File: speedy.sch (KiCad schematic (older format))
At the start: 37 parts, among them U1 STM32F415RGT6, U2 NUF2042VX6, X1 16Mhz 10ppm

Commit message: Change micro USB connector & add 3d models to some footprints
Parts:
- CONN4: footprint _connectors:_Micro-USB-AB-receptacle-SMT -> _connectors:_Micro-USB-AB-receptacle-SMT-th
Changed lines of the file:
@@
 F 0 "CONN4" H 8375 1850 60  0000 C CNN
 F 1 "MICRO_USB" H 8425 1050 60  0000 C CNN
-F 2 "_connectors:_Micro-USB-AB-receptacle-SMT" H 8375 1450 60  0001 C CNN
+F 2 "_connectors:_Micro-USB-AB-receptacle-SMT-th" H 8375 1450 60  0001 C CNN
 F 3 "" H 8375 1450 60  0000 C CNN
 	1    8375 1450

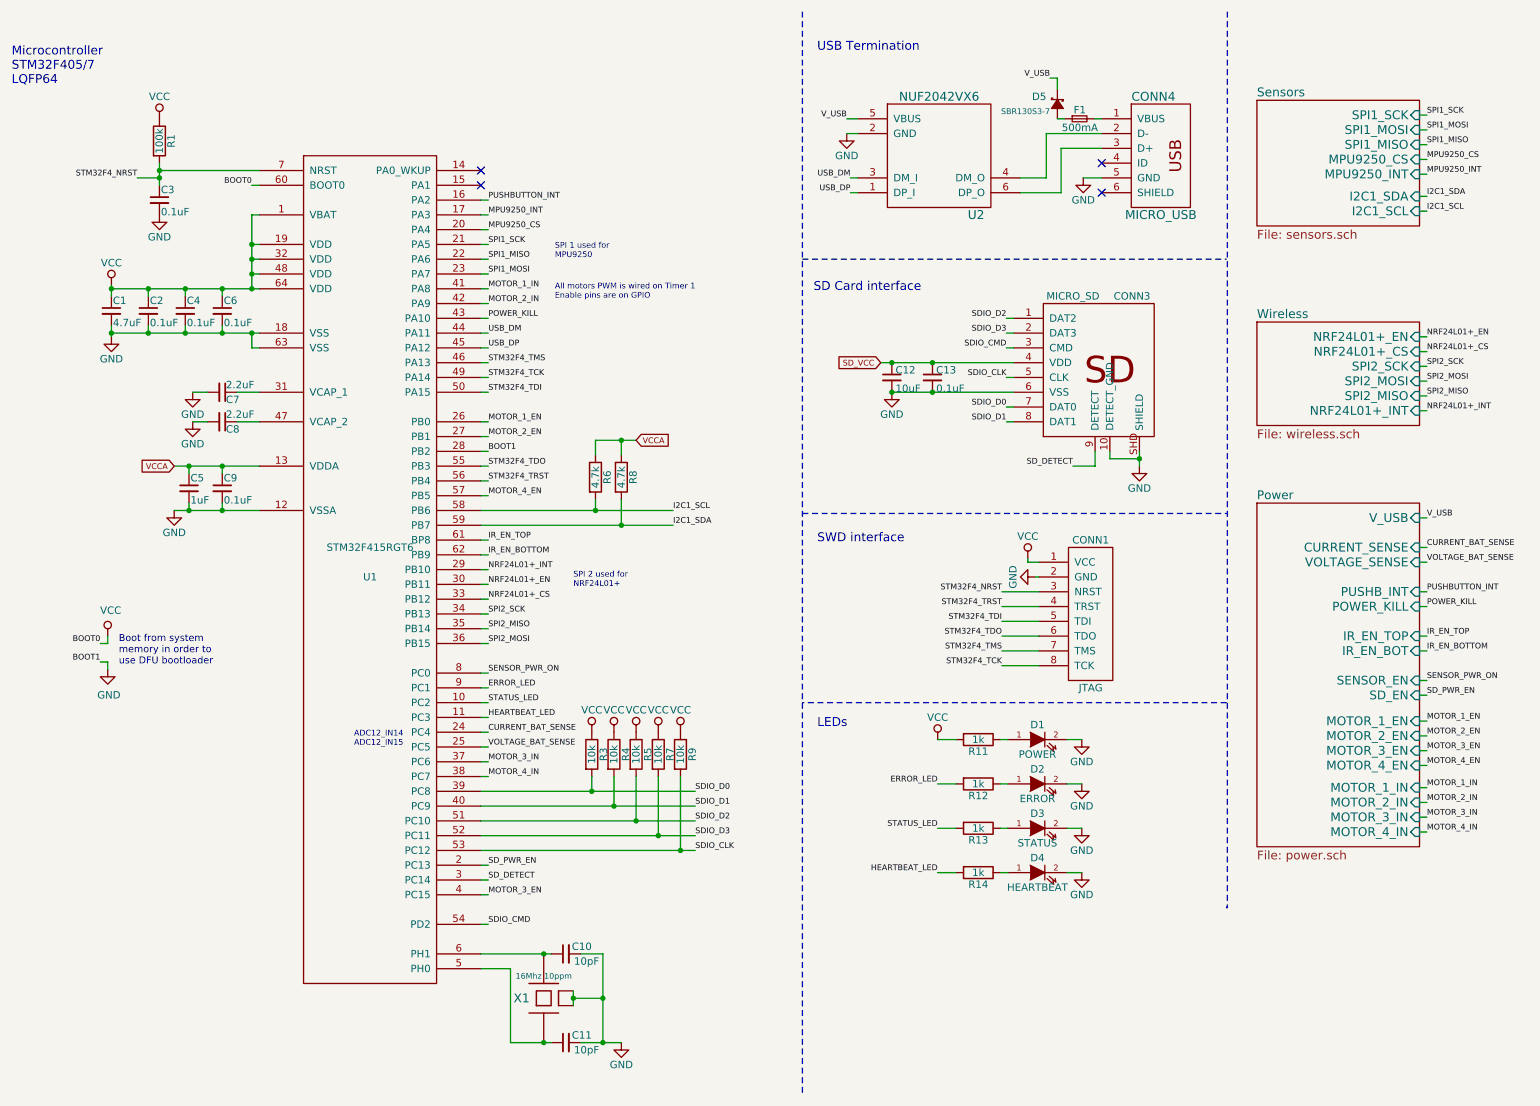
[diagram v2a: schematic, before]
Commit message: Move SDIO pullups from clock to CMD
see NXP AN10911 http://www.nxp.com/documents/application_note/AN10911.pdf
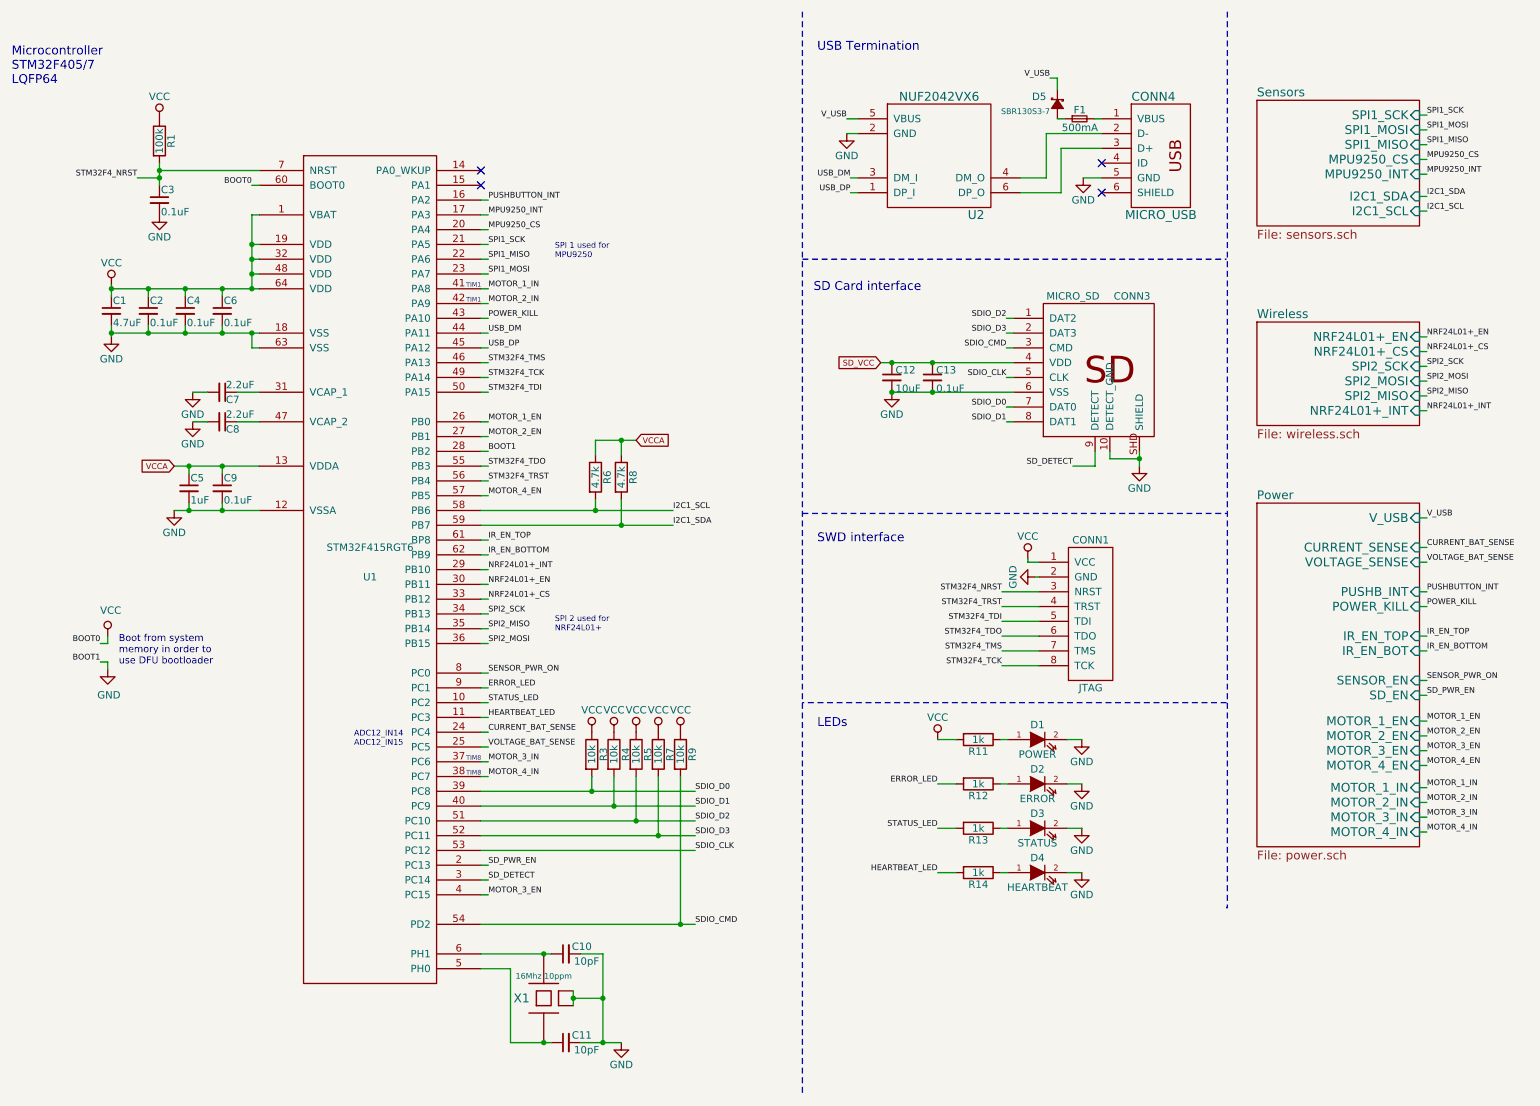
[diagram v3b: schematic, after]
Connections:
- net SDIO_CLK: no longer R9.2
- net SDIO_CMD: now also R9.2
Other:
- note added: "TIM1"
- note added: "TIM8"
- note removed: "All motors PWM is wired on Timer 1\nEnable pins are on GPIO"
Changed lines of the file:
@@
 Text Label 5275 6150 0    39   ~ 0
 SDIO_CLK
-Text Label 3875 6650 0    39   ~ 0
+Text Label 5275 6650 0    39   ~ 0
 SDIO_CMD
 Text Label 3875 6350 0    39   ~ 0
@@
 $EndComp
 $Comp
-L R R9
-U 1 1 5538B6D0
-P 5175 5500
-F 0 "R9" V 5255 5500 50  0000 C CNN
-F 1 "10k" V 5175 5500 50  0000 C CNN
-F 2 "_std:_0402" V 5105 5500 30  0001 C CNN
-F 3 "" H 5175 5500 30  0000 C CNN
-	1    5175 5500
-	1    0    0    -1
-$EndComp
-$Comp
 L VCC #PWR012
 U 1 1 5538C13D
@@
 F 3 "" H 5025 5350 60  0000 C CNN
 	1    5025 5350
-	1    0    0    -1
-$EndComp
-$Comp
-L VCC #PWR016
-U 1 1 5538C2E9
-P 5175 5350
-F 0 "#PWR016" H 5175 5200 50  0001 C CNN
-F 1 "VCC" H 5175 5500 50  0000 C CNN
-F 2 "" H 5175 5350 60  0000 C CNN
-F 3 "" H 5175 5350 60  0000 C CNN
-	1    5175 5350
 	1    0    0    -1
 $EndComp
@@
 Text Label 3875 5650 0    39   ~ 0
 MOTOR_4_IN
-Text Notes 4325 2425 0    39   ~ 0
-All motors PWM is wired on Timer 1\nEnable pins are on GPIO
 Text Notes 4325 2150 0    39   ~ 0
 SPI 1 used for \nMPU9250
@@
 Text Label 3875 4250 0    39   ~ 0
 NRF24L01+_INT
-Text Notes 4450 4375 0    39   ~ 0
+Text Notes 4325 4675 0    39   ~ 0
 SPI 2 used for \nNRF24L01+
 $Comp
@@
 	10175 5275 10225 5275
 Wire Wire Line
-	4450 7100 4450 7200
-Connection ~ 5175 6150
-Wire Wire Line
-	5175 5650 5175 6150
+	4450 7100 4450 7150
+Wire Wire Line
+	4450 7150 4450 7200
 Connection ~ 5025 6050
 Wire Wire Line
@@
 	4575 5650 4575 5750
 Wire Wire Line
-	3825 5950 5275 5950
-Wire Wire Line
-	3825 5850 5275 5850
-Wire Wire Line
-	3825 6050 5275 6050
+	3825 5950 4875 5950
+Wire Wire Line
+	4875 5950 5275 5950
+Wire Wire Line
+	3825 5850 4725 5850
+Wire Wire Line
+	4725 5850 5275 5850
+Wire Wire Line
+	3825 6050 5025 6050
+Wire Wire Line
+	5025 6050 5275 6050
 Wire Wire Line
 	3825 6150 5275 6150
 Wire Wire Line
-	3825 6650 3875 6650
-Wire Wire Line
-	3825 5750 5275 5750
+	3825 6650 5175 6650
+Wire Wire Line
+	5175 6650 5275 6650
+Wire Wire Line
+	3825 5750 4575 5750
+Wire Wire Line
+	4575 5750 5275 5750
 Connection ~ 8280 3500
 Wire Wire Line
@@
 	8080 3450 8080 3500
 Wire Wire Line
-	8280 3450 8280 3550
+	8280 3450 8280 3500
+Wire Wire Line
+	8280 3500 8280 3550
 Wire Wire Line
 	7980 3550 7980 3450
@@
 Connection ~ 6880 3050
 Wire Wire Line
-	6605 3050 7430 3050
+	6605 3050 6880 3050
+Wire Wire Line
+	6880 3050 7430 3050
 Connection ~ 6880 2850
 Wire Wire Line
-	6530 2850 7430 2850
+	6530 2850 6605 2850
+Wire Wire Line
+	6605 2850 6880 2850
+Wire Wire Line
+	6880 2850 7430 2850
 Wire Wire Line
 	7380 3250 7430 3250
@@
 	4600 3775 4600 3850
 Wire Wire Line
-	3825 3850 5125 3850
-Wire Wire Line
-	3825 3950 5125 3950
+	3825 3850 4600 3850
+Wire Wire Line
+	4600 3850 5125 3850
+Wire Wire Line
+	3825 3950 4775 3950
+Wire Wire Line
+	4775 3950 5125 3950
 Connection ~ 4250 7450
 Wire Wire Line
@@
 Connection ~ 4650 7450
 Wire Wire Line
-	4500 7450 4775 7450
-Wire Wire Line
-	4650 6850 4650 7450
-Wire Wire Line
-	4025 7450 4300 7450
-Wire Wire Line
-	3825 6850 4300 6850
+	4500 7450 4650 7450
+Wire Wire Line
+	4650 7450 4775 7450
+Wire Wire Line
+	4650 6850 4650 7150
+Wire Wire Line
+	4650 7150 4650 7450
+Wire Wire Line
+	4025 7450 4250 7450
+Wire Wire Line
+	4250 7450 4300 7450
+Wire Wire Line
+	3825 6850 4250 6850
+Wire Wire Line
+	4250 6850 4300 6850
 Connection ~ 1650 1600
 Wire Wire Line
@@
 	1650 1850 1650 1850
 Wire Wire Line
-	1650 1500 1650 1650
+	1650 1500 1650 1550
+Wire Wire Line
+	1650 1550 1650 1600
+Wire Wire Line
+	1650 1600 1650 1650
 Wire Wire Line
 	2325 1550 1650 1550
@@
 Connection ~ 2075 2350
 Wire Wire Line
-	1325 2325 1325 2400
-Wire Wire Line
-	1325 2600 1325 2675
+	1325 2325 1325 2350
+Wire Wire Line
+	1325 2350 1325 2400
+Wire Wire Line
+	1325 2600 1325 2650
+Wire Wire Line
+	1325 2650 1325 2675
 Wire Wire Line
 	1575 2650 1575 2600
@@
 	6000 475  6000 7800
 Wire Wire Line
-	4600 3375 4875 3375
+	4600 3375 4775 3375
+Wire Wire Line
+	4775 3375 4875 3375
 Connection ~ 4775 3375
 Wire Wire Line
@@
 	2325 1850 2275 1850
 Wire Wire Line
-	2275 1850 2275 2350
+	2275 2350 2275 2250
+Wire Wire Line
+	2275 2250 2275 2150
+Wire Wire Line
+	2275 2150 2275 2050
+Wire Wire Line
+	2275 2050 2275 1850
 Connection ~ 2275 2350
 Wire Wire Line
@@
 Connection ~ 2275 2650
 Wire Wire Line
-	1325 2350 2325 2350
-Wire Wire Line
-	1325 2650 2325 2650
+	1325 2350 1575 2350
+Wire Wire Line
+	1575 2350 1825 2350
+Wire Wire Line
+	1825 2350 2075 2350
+Wire Wire Line
+	2075 2350 2275 2350
+Wire Wire Line
+	2275 2350 2325 2350
+Wire Wire Line
+	1325 2650 1575 2650
+Wire Wire Line
+	1575 2650 1825 2650
+Wire Wire Line
+	1825 2650 2075 2650
+Wire Wire Line
+	2075 2650 2275 2650
+Wire Wire Line
+	2275 2650 2325 2650
 Wire Wire Line
 	2175 3050 2325 3050
@@
 	1875 3050 1975 3050
 Wire Wire Line
-	1750 3550 2325 3550
+	1750 3550 1850 3550
+Wire Wire Line
+	1850 3550 2075 3550
+Wire Wire Line
+	2075 3550 2325 3550
 Wire Wire Line
 	1850 3600 1850 3550
@@
 	1850 3800 1850 3850
 Wire Wire Line
-	1750 3850 2325 3850
+	1750 3850 1850 3850
+Wire Wire Line
+	1850 3850 2075 3850
+Wire Wire Line
+	2075 3850 2325 3850
 Wire Wire Line
 	2075 3850 2075 3800
@@
 Text Notes 1375 4900 0    47   ~ 0
 Boot from system\nmemory in order to \nuse DFU bootloader
+Text Notes 3725 5550 0    31   ~ 0
+TIM8
+Text Notes 3725 2350 0    31   ~ 0
+TIM1
+Text Notes 3725 2450 0    31   ~ 0
+TIM1
+Text Notes 3725 5650 0    31   ~ 0
+TIM8
+$Comp
+L VCC #PWR016
+U 1 1 5538C2E9
+P 5175 5350
+F 0 "#PWR016" H 5175 5200 50  0001 C CNN
+F 1 "VCC" H 5175 5500 50  0000 C CNN
+F 2 "" H 5175 5350 60  0000 C CNN
+F 3 "" H 5175 5350 60  0000 C CNN
+	1    5175 5350
+	1    0    0    -1
+$EndComp
+$Comp
+L R R9
+U 1 1 5538B6D0
+P 5175 5500
+F 0 "R9" V 5255 5500 50  0000 C CNN
+F 1 "10k" V 5175 5500 50  0000 C CNN
+F 2 "_std:_0402" V 5105 5500 30  0001 C CNN
+F 3 "" H 5175 5500 30  0000 C CNN
+	1    5175 5500
+	1    0    0    -1
+$EndComp
+Wire Wire Line
+	5175 5650 5175 6650
+Connection ~ 5175 6650
 $EndSCHEMATC

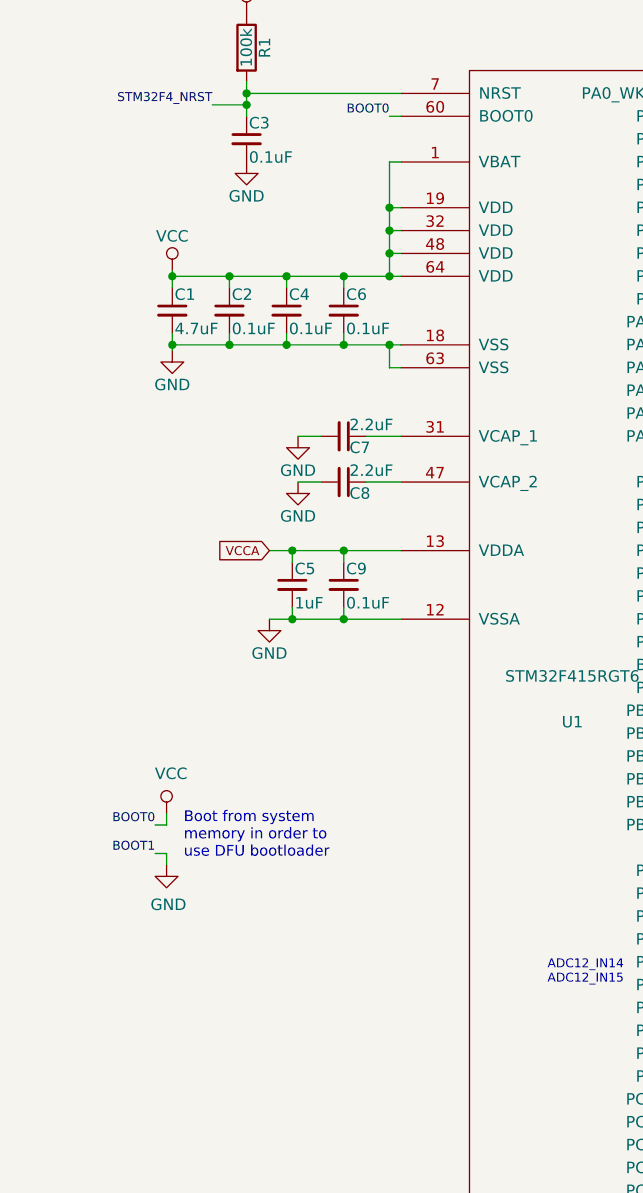
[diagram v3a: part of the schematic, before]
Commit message: Correct boot pattern to enable DFU
Add a push button to VCC on Boot0 to accomplish pattern 1 from AN2606
Previous configuration wouldn't have worked to trigger DFU as noted by @nuft
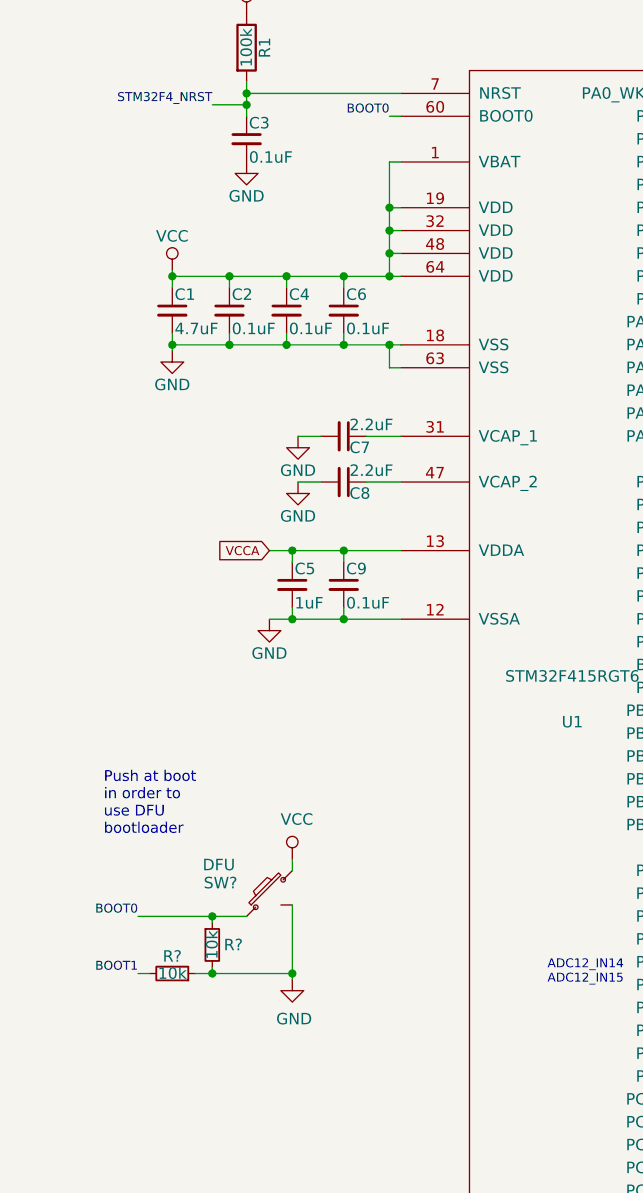
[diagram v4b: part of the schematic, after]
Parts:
- added R? (x2): 10k, symbol R_Small
- added SW?: DFU, symbol PushButton_B3U
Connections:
- net GND: now also R?.1, R?.2, SW?.3 (GND); no longer U1.28 (PB2)
- net VCC: now also SW?.2; no longer U1.60 (BOOT0)
- new net BOOT0: R?.1, SW?.1, U1.60 (BOOT0)
- new net BOOT1: R?.2, U1.28 (PB2)
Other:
- note added: "Push at boot \nin order to\nuse DFU \nbootloader"
- note removed: "Boot from system\nmemory in order to \nuse DFU bootloader"
